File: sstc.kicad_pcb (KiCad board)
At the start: 2 copper layers, 69.5 x 123.8 mm, 50 parts, among them J1 Conn_01x03, J2 Conn_01x03, J3 Conn_01x03, J4 IF-D95T, J5 Conn_01x02, J6 Conn_01x02, Q1 FGA60N65SMD, Q2 FGA60N65SMD, SW1 SW_SPST, T1 Transformer_1P_2S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

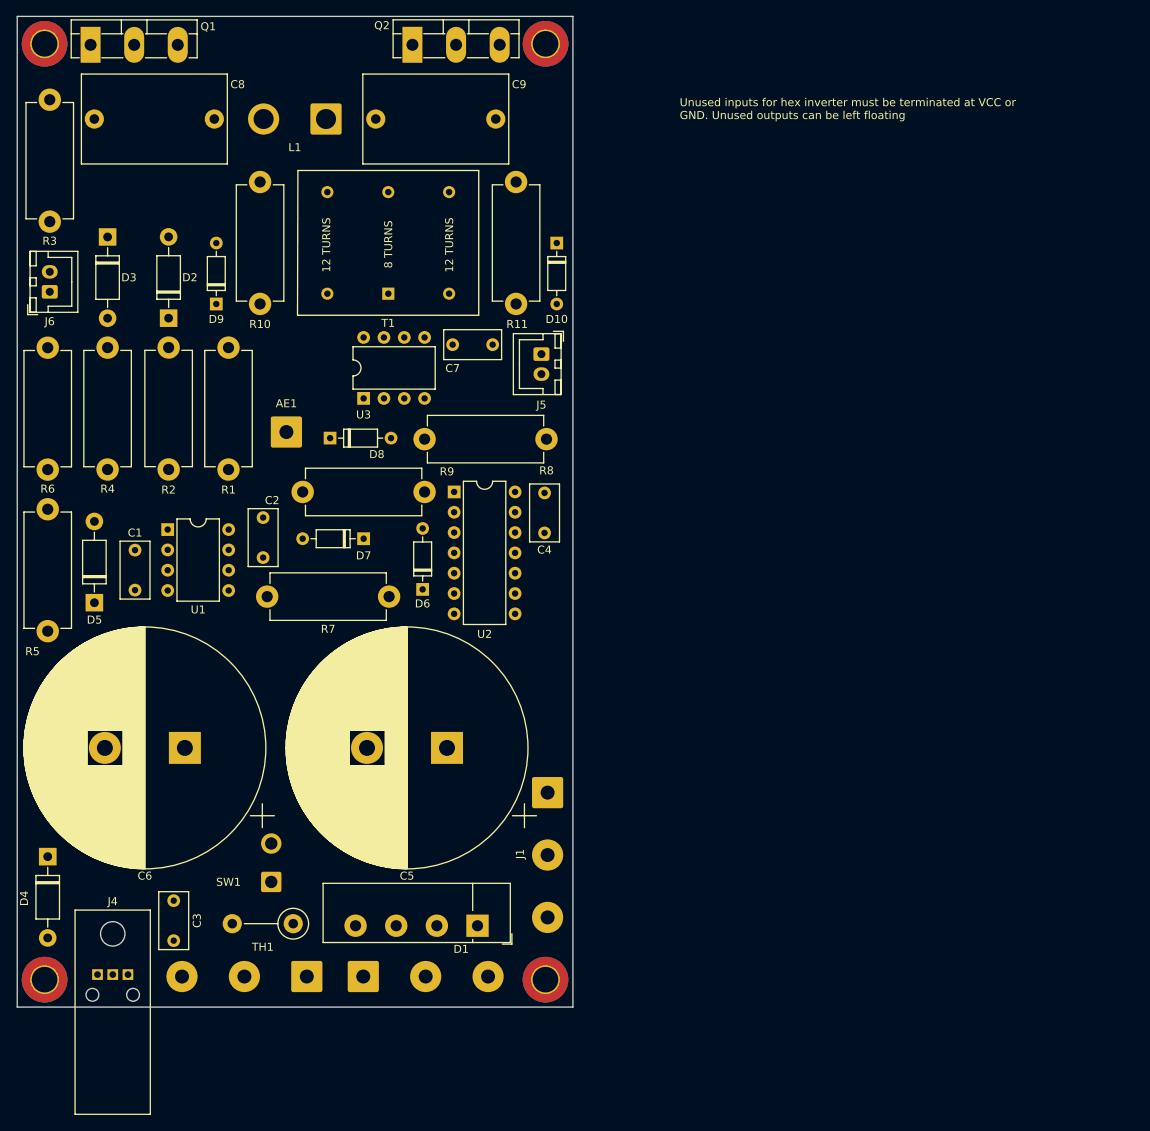
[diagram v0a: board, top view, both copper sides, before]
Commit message: Update schematic and round corners on PCB edge cuts
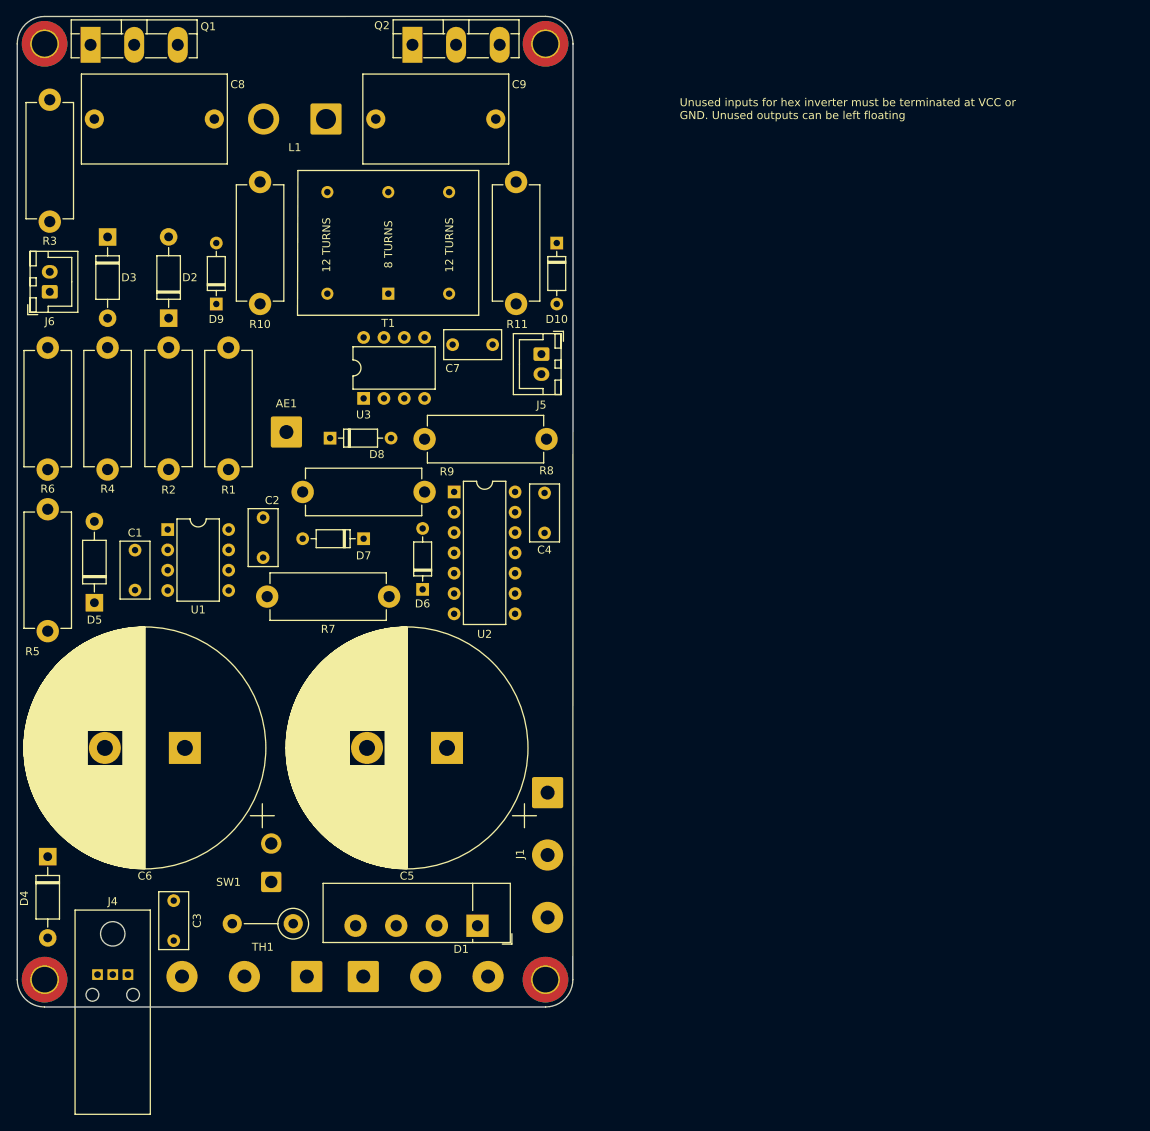
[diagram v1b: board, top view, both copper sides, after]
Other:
- outline, holes or cut-outs redrawn
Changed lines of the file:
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@@
 	)
 	(paper "A4")
+	(title_block
+		(title "Half-Bridge Solid State Tesla Coil (SSTC)")
+		(date "2024-07-30")
+		(company "Newell Jensen")
+	)
 	(layers
 		(0 "F.Cu" signal)
@@
 	)
 	(footprint "MountingHole:MountingHole_3.2mm_M3_ISO7380_Pad_TopBottom"
+		(locked yes)
 		(layer "F.Cu")
 		(at 165.598 151.267 180)
@@
 	)
 	(footprint "MountingHole:MountingHole_3.2mm_M3_ISO7380_Pad_TopBottom"
+		(locked yes)
 		(layer "F.Cu")
 		(at 102.987 151.267 180)
@@
 		)
 	)
-	(gr_rect
-		(start 99.568 30.861)
-		(end 169.027 154.696)
+	(gr_arc
+		(start 102.987 154.686034)
+		(mid 100.574829 153.690061)
+		(end 99.568001 151.2824)
+		(locked yes)
+		(stroke
+			(width 0.05)
+			(type default)
+		)
+		(layer "Edge.Cuts")
+	)
+	(gr_arc
+		(start 99.568 34.29)
+		(mid 100.569402 31.872402)
+		(end 102.987 30.871)
+		(locked yes)
+		(stroke
+			(width 0.05)
+			(type default)
+		)
+		(layer "Edge.Cuts")
+	)
+	(gr_line
+		(start 99.568001 151.2824)
+		(end 99.568 34.29)
+		(locked yes)
+		(stroke
+			(width 0.05)
+			(type default)
+		)
+		(layer "Edge.Cuts")
+	)
+	(gr_arc
+		(start 169.017014 151.267)
+		(mid 168.019141 153.68107)
+		(end 165.608 154.685999)
+		(locked yes)
+		(stroke
+			(width 0.05)
+			(type default)
+		)
+		(layer "Edge.Cuts")
+	)
+	(gr_line
+		(start 165.608 30.861)
+		(end 102.987 30.871)
+		(locked yes)
+		(stroke
+			(width 0.05)
+			(type default)
+		)
+		(layer "Edge.Cuts")
+	)
+	(gr_line
+		(start 169.017014 151.267)
+		(end 169.037 34.29)
+		(locked yes)
+		(stroke
+			(width 0.05)
+			(type default)
+		)
+		(layer "Edge.Cuts")
+	)
+	(gr_line
+		(start 102.987 154.686034)
+		(end 165.608 154.685999)
+		(locked yes)
+		(stroke
+			(width 0.05)
+			(type default)
+		)
+		(layer "Edge.Cuts")
+	)
+	(gr_arc
+		(start 165.608 30.861)
+		(mid 168.032669 31.865331)
+		(end 169.037 34.29)
+		(locked yes)
 		(stroke
-			(width 0.1)
+			(width 0.05)
 			(type default)
 		)
-		(fill none)
 		(layer "Edge.Cuts")
 	)
